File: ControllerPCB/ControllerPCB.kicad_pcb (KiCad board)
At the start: 4 copper layers, 124.5 x 91.5 mm, 187 parts, among them J101 2x4 Pickup Conn, J102 1x4 String Output Conn, J103 Conn_01x03_Pin, J104 Conn_01x03_Pin, J105 Conn_01x03_Pin, J106 Conn_01x03_Pin, J107 USB_B_Micro, J108 10-pin Debug Conn, J109 Conn_01x03_Pin, J201 9V Humbucker OUT, J202 9V IN, J301 MIDI Out Conn, J501 2x20 Conn_1, J502 2x20 Conn_2, U101 STM32F439ZIT6, U201 ADP3336ARMZ, U301 74LVC1G17, Y101 16MHz

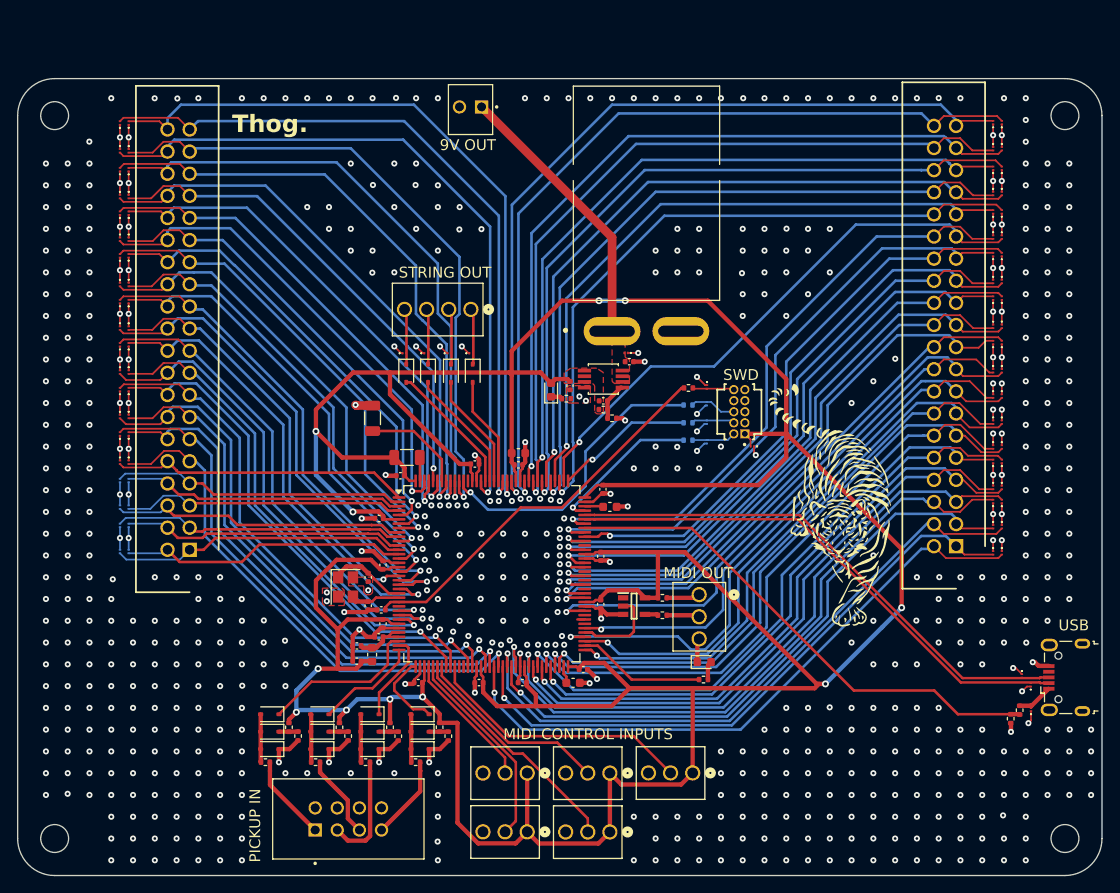
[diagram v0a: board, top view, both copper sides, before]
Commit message: rev 1.05
- new controller is used.
- updated the pcb layout
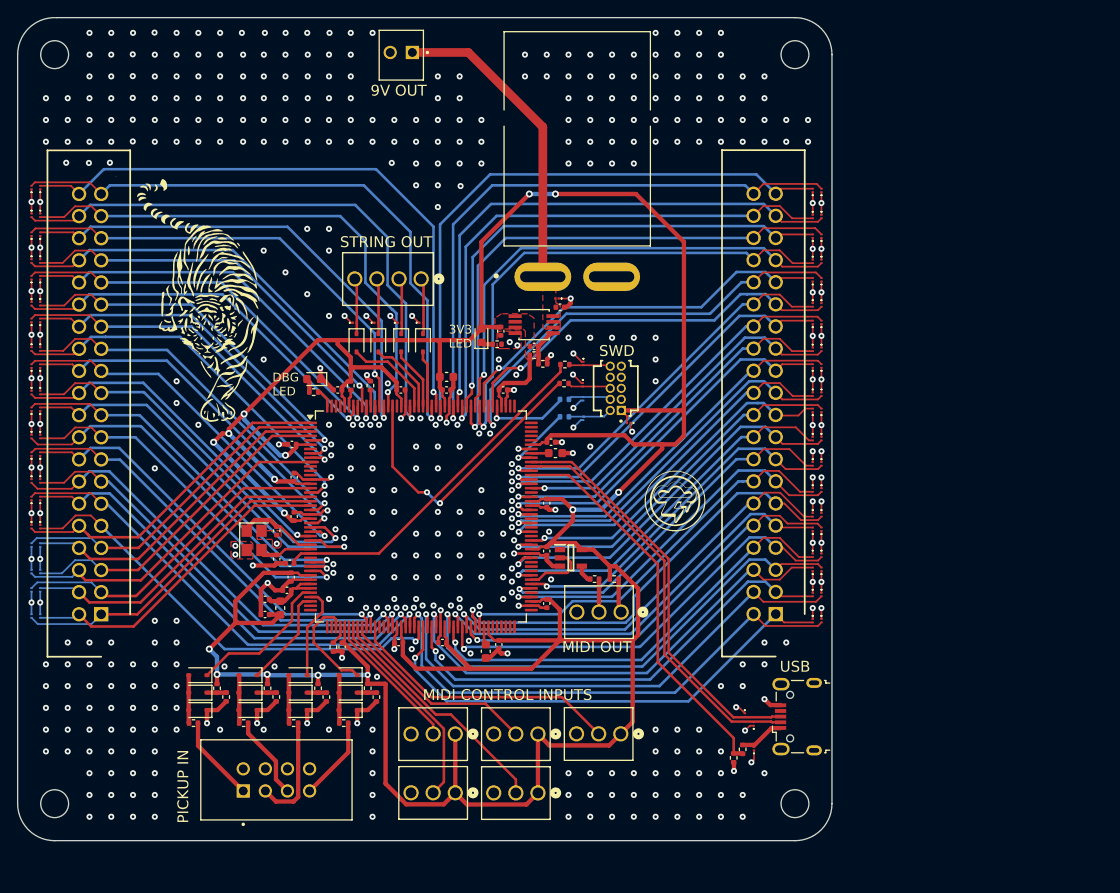
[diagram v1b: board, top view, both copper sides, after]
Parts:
- removed the G*** at (114.2, 86.5)
- removed U101: STM32F439ZIT6, Package_QFP:LQFP-144_20x20mm_P0.5mm
- added C123: 100n, Capacitor_SMD:C_0402_1005Metric, F.Cu at (131.0, 93.5)
- added C124: 100n, Capacitor_SMD:C_0402_1005Metric, F.Cu at (137.5, 93.5)
- added C125: 100n, Capacitor_SMD:C_0402_1005Metric, F.Cu at (143.0, 99.5)
- added G***: LOGO, LOGO, F.Cu at (157.2, 106.2)
- added G***: LOGO, LOGO, B.Cu at (99.2, 74.8)
- added R110: 10k, Resistor_SMD:R_0402_1005Metric, F.Cu at (118.0, 123.0)
- added U102: STM32F437IGT6, Package_QFP:LQFP-176_24x24mm_P0.5mm, F.Cu at (128.1, 108.0)
- D104, R106: moved to F.Cu
- R102, R103: footprint Resistor_SMD:R_1206_3216Metric -> Resistor_SMD:R_0402_1005Metric
- moved H103 140.3 mm to (86.0, 141.0)
- moved H104 90.0 mm to (86.0, 55.0)
- moved H101 85.3 mm to (171.0, 55.0)
- moved G*** 76.2 mm to (102.2, 83.2)
- moved R101 55.6 mm to (115.8, 93.8), turned to 0 degrees
- moved D101 55.4 mm to (115.8, 92.2), turned to 180 degrees
- moved C111 35.7 mm to (118.5, 93.5), turned to 180 degrees
- moved D103 32.1 mm to (165.2, 130.7)
- moved D109 32.1 mm to (166.3, 134.8)
- moved R108 32.1 mm to (165.0, 134.8)
- moved R109 32.1 mm to (164.0, 135.7)
- moved D108 32.1 mm to (166.3, 132.0)
- moved H102 31.3 mm to (171.0, 141.0)
- moved J107 31.1 mm to (171.2, 131.0)
- moved C104 31.0 mm to (113.2, 99.8)
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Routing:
- net +3.3V: track 458.8 -> 424.9 mm, vias 11 -> 15
- net input_71: track 76.0 -> 46.9 mm
- net input_65: track 70.3 -> 41.9 mm
- net input_55: track 69.3 -> 41.1 mm
- net input_72: track 77.6 -> 50.7 mm
- net input_59: track 67.1 -> 40.4 mm
- net input_79: track 96.5 -> 70.0 mm
- net input_80: track 95.2 -> 68.9 mm
- net input_67: track 70.1 -> 44.5 mm
- net input_70: track 69.8 -> 44.2 mm
- net input_66: track 68.2 -> 43.4 mm
- net input_73: track 80.8 -> 56.0 mm
- net input_64: track 68.7 -> 43.9 mm
- net input_63: track 67.8 -> 43.3 mm
- net input_77: track 88.2 -> 63.7 mm
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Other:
- board size 124.5 x 91.5 mm -> 93.5 x 94.5 mm
- board text added: "3V3 LED"
- board text added: "DBG LED"
- board text added: "KRAKEN"
- board text removed: "Thog."
